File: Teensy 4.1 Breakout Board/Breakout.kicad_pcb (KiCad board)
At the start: 2 copper layers, 145 x 64.5 mm, 20 parts, among them J1 CAN1, J2 CAN2, J3 12V_IN, J4 APPS, J5 BRAKE_PRESSURE_IN, J6 BRAKE_LIGHT_OUT, J7 3.3V_OUT, J8 GND_COMMON, M3 MountingHole_3.2mm_M3_Pad, Q1 IRLZ44N, U1 Teensy4.1, U2 MCP2562-E-P, U3 LM2596S-5, U4 MCP2562-E-P

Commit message: breakout board v1 sizing
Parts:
- removed M3 (x4): MountingHole_3.2mm_M3_Pad, MountingHole:MountingHole_3.2mm_M3_Pad
- removed U4: MCP2562-E-P, Package_DIP:DIP-8_W7.62mm
- added C1: 0.1uF, FA14_Capacitor:FA18X7R1H104KNU00, F.Cu at (156.3, 88.0)
- added C15: 220uF, Capacitor_THT:CP_Radial_D6.3mm_P2.50mm, F.Cu at (151.3, 113.6)
- added C18: 680uF, footprints:CAPPRD500W60D1275H2700, F.Cu at (163.4, 123.8)
- added C2: 0.1uF, FA14_Capacitor:FA18X7R1H104KNU00, F.Cu at (192.1, 114.2)
- added C3: 0.1uF, FA14_Capacitor:FA18X7R1H104KNU00, F.Cu at (152.5, 89.9)
- added C5: 0.1uF, FA14_Capacitor:FA18X7R1H104KNU00, F.Cu at (182.0, 90.5)
- added C6: 0.1uF, FA14_Capacitor:FA18X7R1H104KNU00, F.Cu at (178.5, 90.5)
- added C7: 0.1uF, FA14_Capacitor:FA18X7R1H104KNU00, F.Cu at (175.0, 90.5)
- added C8: 0.1uF, FA14_Capacitor:FA18X7R1H104KNU00, F.Cu at (171.5, 90.5)
- added C9: 10uF, Capacitor_THT:CP_Radial_D5.0mm_P2.50mm, F.Cu at (152.6, 85.3)
- added D1: NUP3105L, Package_TO_SOT_SMD:SOT-23, F.Cu at (156.7, 84.6)
- added D3: 1N5821, Diode_THT:D_DO-201AD_P15.24mm_Horizontal, F.Cu at (176.8, 134.3)
- added J10: RTD_Speaker, Connector_JST:JST_XH_B2B-XH-A_1x02_P2.50mm_Vertical, F.Cu at (187.8, 118.9)
- added J9: Brake_Light, Connector_JST:JST_XH_B2B-XH-A_1x02_P2.50mm_Vertical, F.Cu at (187.8, 126.3)
- added JP1: SolderJumper_2_Open, Jumper:SolderJumper-2_P1.3mm_Open_Pad1.0x1.5mm, F.Cu at (167.8, 89.3)
- added L1: 33uH, Inductor_SMD:L_10.4x10.4_H4.8, F.Cu at (178.8, 123.7)
- added Q2: 2N7000, Package_TO_SOT_THT:TO-92_Inline, F.Cu at (187.7, 114.2)
- added R10: 20k, Resistor_THT:R_Axial_DIN0207_L6.3mm_D2.5mm_P10.16mm_Horizontal, F.Cu at (186.5, 82.5)
- added R11: 10k, Resistor_THT:R_Axial_DIN0207_L6.3mm_D2.5mm_P10.16mm_Horizontal, F.Cu at (209.7, 86.0)
- added R12: 20k, Resistor_THT:R_Axial_DIN0207_L6.3mm_D2.5mm_P10.16mm_Horizontal, F.Cu at (199.5, 89.5)
- added R13: 1k, Resistor_THT:R_Axial_DIN0207_L6.3mm_D2.5mm_P10.16mm_Horizontal, F.Cu at (183.7, 78.0)
- added R14: 1k, Resistor_THT:R_Axial_DIN0207_L6.3mm_D2.5mm_P10.16mm_Horizontal, F.Cu at (183.7, 81.5)
- added R15: 1k, Resistor_THT:R_Axial_DIN0207_L6.3mm_D2.5mm_P10.16mm_Horizontal, F.Cu at (183.7, 85.0)
- added R16: 1k, Resistor_THT:R_Axial_DIN0207_L6.3mm_D2.5mm_P10.16mm_Horizontal, F.Cu at (170.7, 80.1)
- added R4: 20k, Resistor_THT:R_Axial_DIN0207_L6.3mm_D2.5mm_P10.16mm_Horizontal, F.Cu at (199.4, 82.5)
- added R5: 100, Resistor_THT:R_Axial_DIN0207_L6.3mm_D2.5mm_P10.16mm_Horizontal, F.Cu at (155.0, 111.9)
- added R6: 100k, Resistor_THT:R_Axial_DIN0207_L6.3mm_D2.5mm_P10.16mm_Horizontal, F.Cu at (155.0, 115.4)
- added R7: 100, Resistor_THT:R_Axial_DIN0207_L6.3mm_D2.5mm_P10.16mm_Horizontal, F.Cu at (173.1, 112.3)
- added R8: 100k, Resistor_THT:R_Axial_DIN0207_L6.3mm_D2.5mm_P10.16mm_Horizontal, F.Cu at (173.1, 115.7)
- added R9: 10k, Resistor_THT:R_Axial_DIN0207_L6.3mm_D2.5mm_P10.16mm_Horizontal, F.Cu at (196.7, 79.0)
- added REF**: MountingHole_3.2mm_M3, MountingHole:MountingHole_3.2mm_M3, F.Cu at (143.4, 100.8)
- added REF**: MountingHole_3.2mm_M3, MountingHole:MountingHole_3.2mm_M3, F.Cu at (143.4, 79.3)
- added REF**: MountingHole_3.2mm_M3, MountingHole:MountingHole_3.2mm_M3, F.Cu at (214.8, 100.8)
- added REF**: MountingHole_3.2mm_M3, MountingHole:MountingHole_3.2mm_M3, F.Cu at (143.4, 133.6)
- added REF**: MountingHole_3.2mm_M3, MountingHole:MountingHole_3.2mm_M3, F.Cu at (214.8, 133.6)
- added REF**: MountingHole_2.7mm_M2.5, MountingHole:MountingHole_2.7mm_M2.5, F.Cu at (208.1, 113.0)
- added REF**: MountingHole_3.2mm_M3, MountingHole:MountingHole_3.2mm_M3, F.Cu at (214.8, 79.3)
- added REF**: MountingHole_2.7mm_M2.5, MountingHole:MountingHole_2.7mm_M2.5, F.Cu at (208.1, 129.0)
- added R_CAN_TERM1: 120, Resistor_THT:R_Axial_DIN0207_L6.3mm_D2.5mm_P10.16mm_Horizontal, F.Cu at (160.5, 83.7)
- added U26: LM2596SX-5.0/NOPB, Package_TO_SOT_SMD:TO-263-5_TabPin3, F.Cu at (153.1, 128.7)
- J1: value CAN1 -> CAN; footprint TerminalBlock_Phoenix:TerminalBlock_Phoenix_MKDS-1,5-2-5.08_1x02_P5.08mm_Horizontal -> Connector_JST:JST_XH_B3B-XH-A_1x03_P2.50mm_Vertical
- J2: value CAN2 -> 12V Power; footprint TerminalBlock_Phoenix:TerminalBlock_Phoenix_MKDS-1,5-2-5.08_1x02_P5.08mm_Horizontal -> Connector_JST:JST_XH_B2B-XH-A_1x02_P2.50mm_Vertical
- J3: value 12V_IN -> APPS1; footprint TerminalBlock_Phoenix:TerminalBlock_Phoenix_MKDS-1,5-2-5.08_1x02_P5.08mm_Horizontal -> Connector_JST:JST_XH_B3B-XH-A_1x03_P2.50mm_Vertical
- J4: value APPS -> APPS2; footprint TerminalBlock_Phoenix:TerminalBlock_Phoenix_MKDS-1,5-2-5.08_1x02_P5.08mm_Horizontal -> Connector_JST:JST_XH_B3B-XH-A_1x03_P2.50mm_Vertical
- J5: value BRAKE_PRESSURE_IN -> Brake_Pressure_Front; footprint TerminalBlock_Phoenix:TerminalBlock_Phoenix_MKDS-1,5-2-5.08_1x02_P5.08mm_Horizontal -> Connector_JST:JST_XH_B3B-XH-A_1x03_P2.50mm_Vertical
- J6: value BRAKE_LIGHT_OUT -> Brake_Pressure_Rear; footprint TerminalBlock_Phoenix:TerminalBlock_Phoenix_MKDS-1,5-2-5.08_1x02_P5.08mm_Horizontal -> Connector_JST:JST_XH_B3B-XH-A_1x03_P2.50mm_Vertical
- J7: value 3.3V_OUT -> Nextion; footprint TerminalBlock_Phoenix:TerminalBlock_Phoenix_MKDS-1,5-4-5.08_1x04_P5.08mm_Horizontal -> Connector_JST:JST_XH_B4B-XH-A_1x04_P2.50mm_Vertical
- J8: value GND_COMMON -> ESP32; footprint TerminalBlock_Phoenix:TerminalBlock_Phoenix_MKDS-1,5-4-5.08_1x04_P5.08mm_Horizontal -> Connector_JST:JST_XH_B4B-XH-A_1x04_P2.50mm_Vertical
- Q1: value IRLZ44N -> 2N7000; footprint Package_TO_SOT_THT:TO-220-3_Vertical -> Package_TO_SOT_THT:TO-92_Inline
- R1: value 120 -> 10k; footprint Resistor_SMD:R_0603_1608Metric -> Resistor_THT:R_Axial_DIN0207_L6.3mm_D2.5mm_P10.16mm_Horizontal
- R2: value 120 -> 20k; footprint Resistor_SMD:R_0603_1608Metric -> Resistor_THT:R_Axial_DIN0207_L6.3mm_D2.5mm_P10.16mm_Horizontal
- R3: value 10K -> 10k; footprint Resistor_SMD:R_0603_1608Metric -> Resistor_THT:R_Axial_DIN0207_L6.3mm_D2.5mm_P10.16mm_Horizontal
- U1: value Teensy4.1 -> SN65HVD230; footprint teensy:Teensy41 -> Package_SO:SOIC-8_3.9x4.9mm_P1.27mm
- U2: value MCP2562-E-P -> module_mpu6050; footprint Package_DIP:DIP-8_W7.62mm -> usini_sensors:module_mpu6050
- U3: value LM2596S-5 -> Teensy4.1; footprint Package_TO_SOT_SMD:TO-263-5_TabPin3 -> teensy.pretty-master:Teensy41
- moved J3 188.6 mm to (214.5, 125.2), turned to 90 degrees
- moved R2 148.6 mm to (186.5, 89.5)
- moved R1 143.1 mm to (196.7, 86.0), turned to 180 degrees
- moved U2 141.7 mm to (195.4, 130.0), turned to 0 degrees
- moved U3 128.8 mm to (179.3, 100.8), turned to 0 degrees
- moved J6 121.9 mm to (214.7, 91.9), turned to 90 degrees
- moved J4 119.6 mm to (214.5, 113.7), turned to 90 degrees
- moved J2 109.6 mm to (143.3, 123.0), turned to -90 degrees
- moved J1 106.7 mm to (155.6, 79.1), turned to 180 degrees
- moved J8 95.9 mm to (183.0, 133.9), turned to 0 degrees
- moved U1 60.3 mm to (162.3, 88.4), turned to 0 degrees
- moved R3 58.9 mm to (209.5, 79.0), turned to 180 degrees
- moved J5 39.0 mm to (144.2, 86.8), turned to -90 degrees
- moved Q1 37.5 mm to (169.5, 114.9), turned to 90 degrees
- moved J7 8.22 mm to (143.3, 108.9), turned to -90 degrees
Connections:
- J1 pad 1: Net-(J1-Pin_1) -> CAN_GND
- J1 pad 2: Net-(J1-Pin_2) -> CANL
- J2 pad 1: Net-(J2-Pin_1) -> 12V
- J2 pad 2: Net-(J2-Pin_2) -> CAN_GND
- J3 pad 1: Net-(J3-Pin_1) -> 5V
- J3 pad 2: /BRAKE_LIGHT_12V -> APPS1
- J4 pad 1: /APPS1 -> 5V
- J4 pad 2: /APPS2 -> APPS2
- J5 pad 1: /FRONT_BRAKE_PRESSURE -> 5V
- J5 pad 2: /REAR_BRAKE_PRESSURE -> Brake_Front
- J6 pad 1: Net-(J6-Pin_1) -> 5V
- J6 pad 2: /BRAKE_LIGHT_12V -> Brake_Rear
- J7 pad 1: /3.3V -> 5V
- J7 pad 2: /3.3V -> Nextion_TX
- J7 pad 3: /3.3V -> Nextion_RX
- J7 pad 4: /3.3V -> CAN_GND
- J8 pad 1: /GND -> 5V
- J8 pad 2: /GND -> ESP32_TX
- J8 pad 3: /GND -> ESP32_RX
- J8 pad 4: /GND -> CAN_GND
- Q1 pad 1: /BRAKE_LIGHT_CONTROL -> CAN_GND
- Q1 pad 2: Net-(J6-Pin_1) -> Net-(Q1-G)
- Q1 pad 3: /GND -> Net-(J9-Pin_2)
- R1 pad 1: Net-(J1-Pin_1) -> APPS1
- R1 pad 2: Net-(J1-Pin_2) -> Net-(R1-Pad2)
- R2 pad 1: Net-(J2-Pin_1) -> Net-(R1-Pad2)
- R2 pad 2: Net-(J2-Pin_2) -> CAN_GND
- R3 pad 1: /GND -> APPS2
- R3 pad 2: /BRAKE_LIGHT_CONTROL -> Net-(R14-Pad2)
- U1 pad 1: /GND -> CAN1_TX
- U1 pad 2: /CAN2_RX -> CAN_GND
- U1 pad 3: /CAN2_TX -> 3.3V
- U1 pad 4: /BRAKE_LIGHT_CONTROL -> CAN1_RX
- U1 pad 6: unconnected-(U1-4_BCLK2-Pad6) -> CANL
- U1 pad 7: unconnected-(U1-5_IN2-Pad7) -> CANH
- U1 pad 8: unconnected-(U1-6_OUT1D-Pad8) -> CAN_GND
- U2 pad 1: /CAN1_TX -> 3.3V
- U2 pad 2: /GND -> CAN_GND
- U2 pad 3: /5V -> MPU_SCL
- U2 pad 4: /CAN1_RX -> MPU_SDA
- U2 pad 5: /3.3V -> unconnected-(U2-XDA-Pad5)
- U2 pad 6: Net-(J1-Pin_2) -> unconnected-(U2-XCL-Pad6)
- U2 pad 7: Net-(J1-Pin_1) -> unconnected-(U2-ADD-Pad7)
- U2 pad 8: /GND -> unconnected-(U2-INT-Pad8)
- U3 pad 1: /BRAKE_LIGHT_12V -> unconnected-(U3-GND-Pad1)
- U3 pad 2: /5V -> Nextion_TX
- U3 pad 3: Net-(J3-Pin_1) -> Nextion_RX
- U3 pad 5: Net-(J3-Pin_1) -> unconnected-(U3-3_LRCLK2-Pad5)
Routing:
- net /5V: track 273.5 -> 0.00 mm
- net /GND: track 165.2 -> 0.00 mm
- net /CAN1_RX: track 149.8 -> 0.00 mm
- net /3.3V: track 132.8 -> 0.00 mm
- net /CAN2_RX: track 127.3 -> 0.00 mm
- net /CAN2_TX: track 110.3 -> 0.00 mm
- net Net-(J6-Pin_1): track 64.9 -> 0.00 mm
- net /BRAKE_LIGHT_12V: track 63.4 -> 0.00 mm
- net /CAN1_TX: track 62.3 -> 0.00 mm
- net /BRAKE_LIGHT_CONTROL: track 45.7 -> 0.00 mm
- net Net-(J3-Pin_1): track 27.1 -> 0.00 mm
- net Net-(J2-Pin_2): track 25.1 -> 0.00 mm
- net Net-(J2-Pin_1): track 21.3 -> 0.00 mm
- net /APPS1: track 17.9 -> 0.00 mm
- net /REAR_BRAKE_PRESSURE: track 17.2 -> 0.00 mm
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- added copper zone on F.Cu, net CAN_GND
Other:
- board size 145 x 64.5 mm -> 81.4 x 64.3 mm
- board text removed: "UCDFS TEENSY 4.1 BREAKOUT BOARD"

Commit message: breakout complete
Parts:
- moved R5 10.2 mm to (165.2, 111.9), turned to 180 degrees
- moved Q1 2.71 mm to (168.9, 112.3), turned to -90 degrees
- moved C9 2.71 mm to (149.9, 85.4), turned to 0 degrees
- moved Q2 2.50 mm to (187.3, 111.7), turned to -90 degrees
- moved C15 2.48 mm to (148.8, 113.6), turned to 0 degrees
- moved C5 0.22 mm to (182.2, 90.4)
- moved C6 0.22 mm to (178.7, 90.4)
- moved C7 0.22 mm to (175.2, 90.4)
- moved C8 0.22 mm to (171.7, 90.4)
- moved R6 0.10 mm to (155.0, 115.3)
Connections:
- J1 pad 2: CANL -> CANH
- J1 pad 3: CANH -> CANL
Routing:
- net 5V: track 0.00 -> 170.7 mm
- net Brake_Front: track 0.00 -> 60.9 mm
- net 3.3V: track 0.00 -> 60.5 mm
- net 12V: track 0.00 -> 57.6 mm
- net APPS1: track 0.00 -> 48.3 mm
- net Net-(R11-Pad2): track 0.00 -> 48.0 mm
- net MPU_SDA: track 0.00 -> 45.8 mm
- net MPU_SCL: track 0.00 -> 43.8 mm
- net Net-(D3-K): track 0.00 -> 38.1 mm
- net APPS2: track 0.00 -> 34.3 mm
- net ESP32_TX: track 0.00 -> 32.3 mm
- net ESP32_RX: track 0.00 -> 31.7 mm
- net Net-(R14-Pad2): track 0.00 -> 30.9 mm
- net Net-(J9-Pin_2): track 0.00 -> 26.6 mm
- net CANL: track 0.00 -> 22.9 mm
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
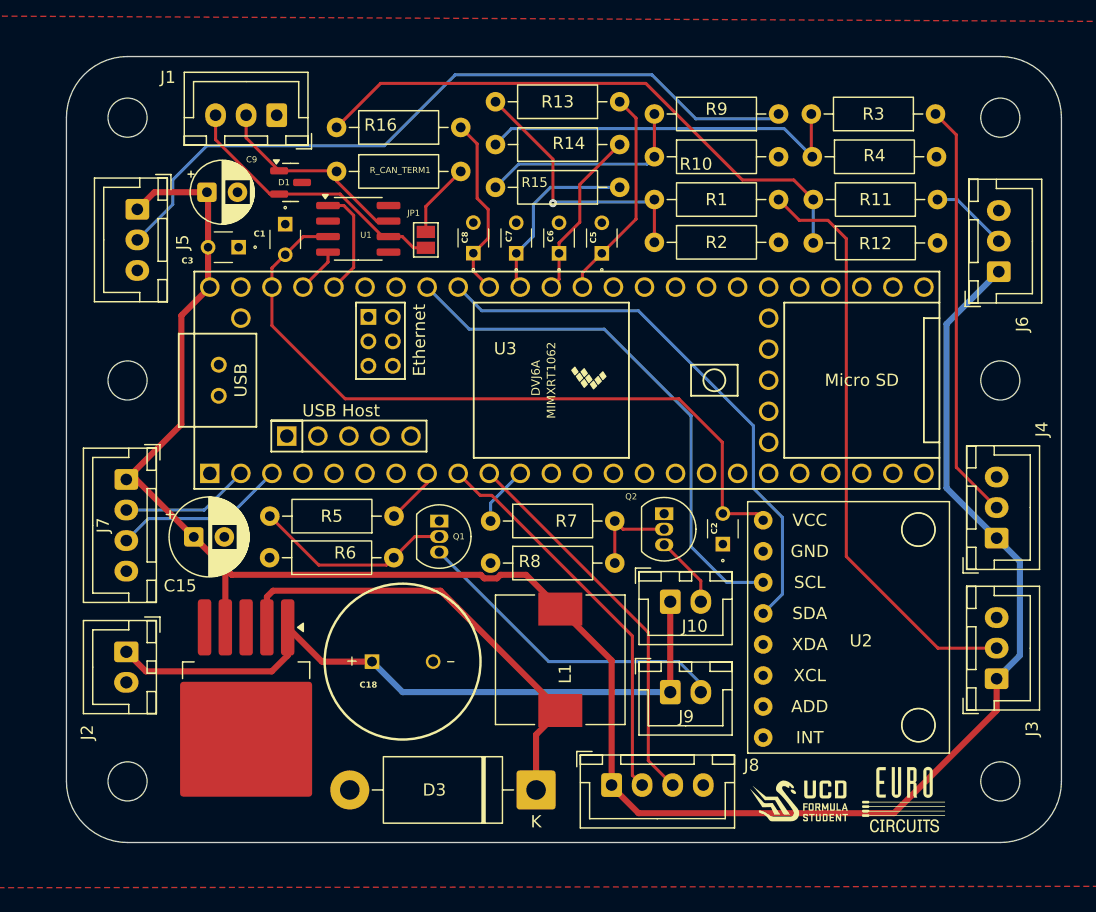
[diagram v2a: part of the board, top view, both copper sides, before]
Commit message: breakout updated and ENNOID BMS added
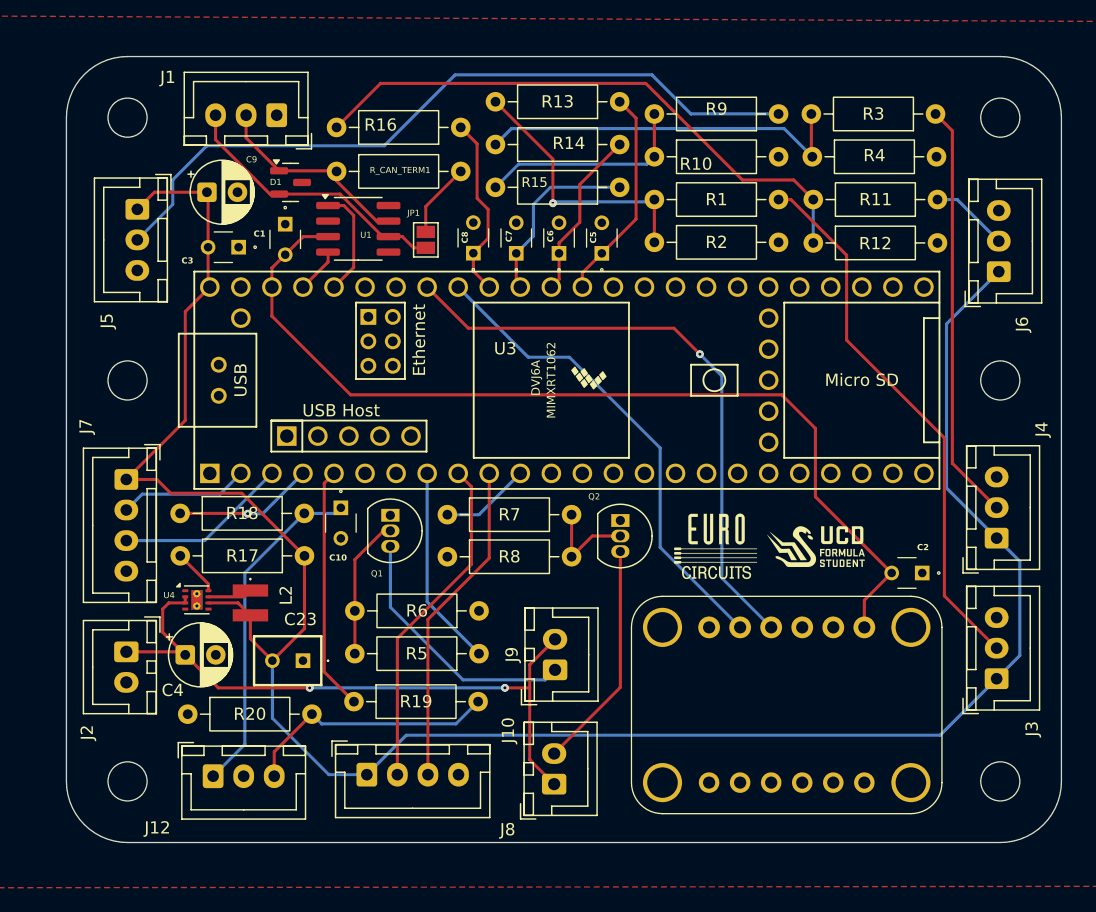
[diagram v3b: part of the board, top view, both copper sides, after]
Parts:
- removed C15: 220uF, Capacitor_THT:CP_Radial_D6.3mm_P2.50mm
- removed C18: 680uF, footprints:CAPPRD500W60D1275H2700
- removed D3: 1N5821, Diode_THT:D_DO-201AD_P15.24mm_Horizontal
- removed L1: 33uH, Inductor_SMD:L_10.4x10.4_H4.8
- removed the REF** at (208.1, 113.0)
- removed the REF** at (208.1, 129.0)
- removed U2: module_mpu6050, usini_sensors:module_mpu6050
- removed U26: LM2596SX-5.0/NOPB, Package_TO_SOT_SMD:TO-263-5_TabPin3
- added C10: 0.1uF, FA14_Capacitor:FA18X7R1H104KNU00, F.Cu at (160.8, 111.2)
- added C23: 22uF, RDEC71E:RDEC71E226K3P1H03B, F.Cu at (157.8, 123.7)
- added C4: 10uF, Capacitor_THT:CP_Radial_D5.0mm_P2.50mm, F.Cu at (148.1, 123.2)
- added J12: RTD_button, Connector_JST:JST_XH_B3B-XH-A_1x03_P2.50mm_Vertical, F.Cu at (150.4, 133.2)
- added L2: 2.2uH, XFL3012222:XFL3012222MEC, F.Cu at (153.4, 119.0)
- added R17: 100k, Resistor_THT:R_Axial_DIN0207_L6.3mm_D2.5mm_P10.16mm_Horizontal, F.Cu at (157.9, 115.2)
- added R18: 220, Resistor_THT:R_Axial_DIN0207_L6.3mm_D2.5mm_P10.16mm_Horizontal, F.Cu at (147.7, 111.7)
- added R19: 100, Resistor_THT:R_Axial_DIN0207_L6.3mm_D2.5mm_P10.16mm_Horizontal, F.Cu at (161.9, 127.1)
- added R20: 100k, Resistor_THT:R_Axial_DIN0207_L6.3mm_D2.5mm_P10.16mm_Horizontal, F.Cu at (148.3, 128.1)
- added U4: TPS62163DSG, Package_SON:WSON-8-1EP_2x2mm_P0.5mm_EP0.9x1.6mm_ThermalVias, F.Cu at (149.1, 118.8)
- added U5: MPU6050, adafruit:MPU6050, F.Cu at (200.7, 129.6)
- moved J8 20.0 mm to (163.0, 133.1)
- moved J10 17.7 mm to (178.3, 133.8), turned to 90 degrees
- moved R6 17.7 mm to (172.2, 119.7), turned to 180 degrees
- moved C2 16.5 mm to (208.4, 116.5), turned to 180 degrees
- moved R5 13.2 mm to (172.2, 123.2)
- moved J9 9.60 mm to (178.4, 124.5), turned to 90 degrees
- moved Q1 4.03 mm to (164.9, 111.8)
- moved Q2 3.63 mm to (183.7, 112.3)
- moved R7 3.57 mm to (169.6, 111.8)
- moved R8 3.57 mm to (169.6, 115.2)
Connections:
- J9 pad 1: 12V -> Net-(J9-Pin_1)
- J9 pad 2: Net-(J9-Pin_2) -> 12V
- Q1 pad 3: Net-(J9-Pin_2) -> Net-(J9-Pin_1)
- U3 pad 4: unconnected-(U3-2_OUT2-Pad4) -> RTD_button
- U3 pad 5: unconnected-(U3-3_LRCLK2-Pad5) -> Precharge_EN
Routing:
- net Net-(D3-K): track 38.1 -> 0.00 mm
- net Net-(J12-Pin_1): track 0.00 -> 27.8 mm
- net Net-(J9-Pin_2): track 26.6 -> 0.00 mm
- net Net-(J9-Pin_1): track 0.00 -> 21.3 mm
- net Net-(J12-Pin_3): track 0.00 -> 21.0 mm
- net Precharge_EN: track 0.00 -> 20.0 mm
- net 3.3V: track 60.5 -> 77.6 mm
- net Net-(J10-Pin_2): track 5.93 -> 18.8 mm
- net Brake_Light_EN: track 4.62 -> 16.5 mm
- net RTD_button: track 0.00 -> 11.4 mm, vias 0 -> 1
- net MPU_SDA: track 45.8 -> 39.4 mm
- net MPU_SCL: track 43.8 -> 49.4 mm, vias 0 -> 1
- net ESP32_RX: track 31.7 -> 26.7 mm
- net Net-(Q1-G): track 16.5 -> 11.6 mm
- net ESP32_TX: track 32.3 -> 27.6 mm
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
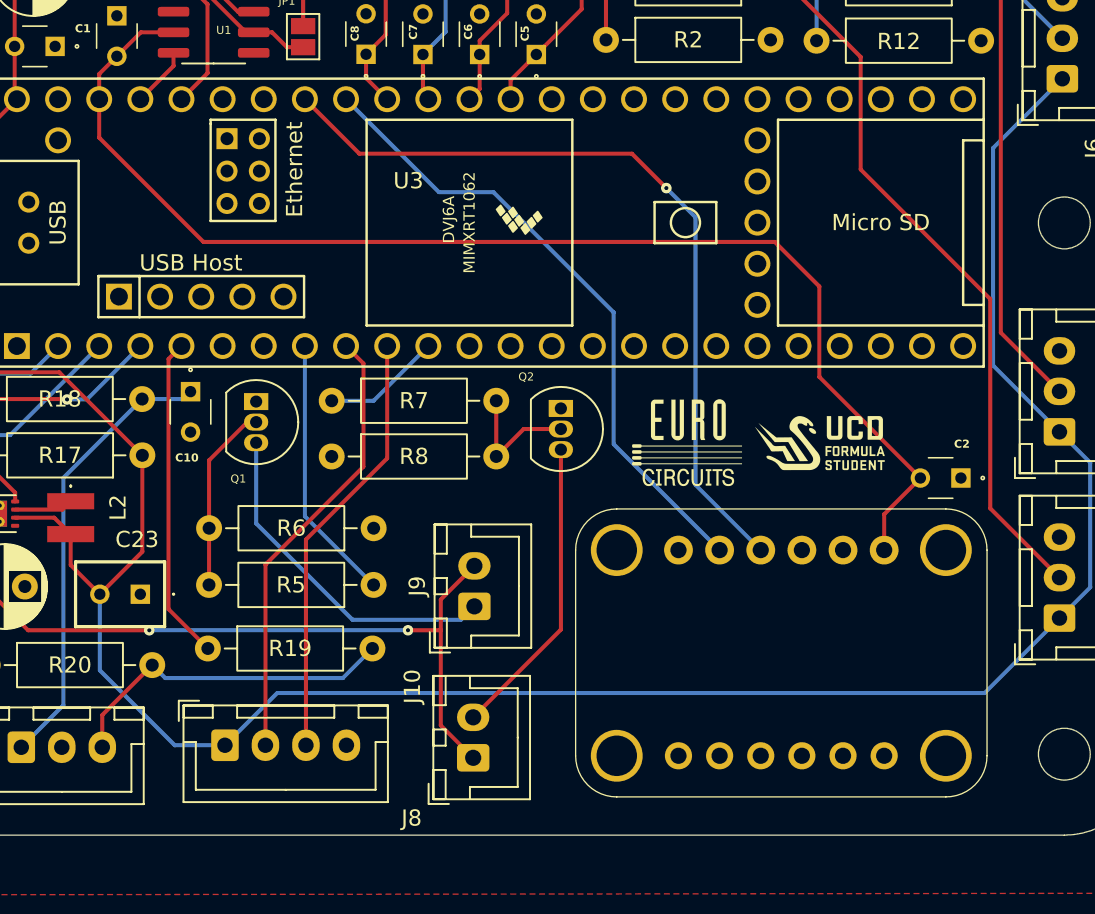
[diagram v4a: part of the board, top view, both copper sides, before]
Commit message: updated breakout
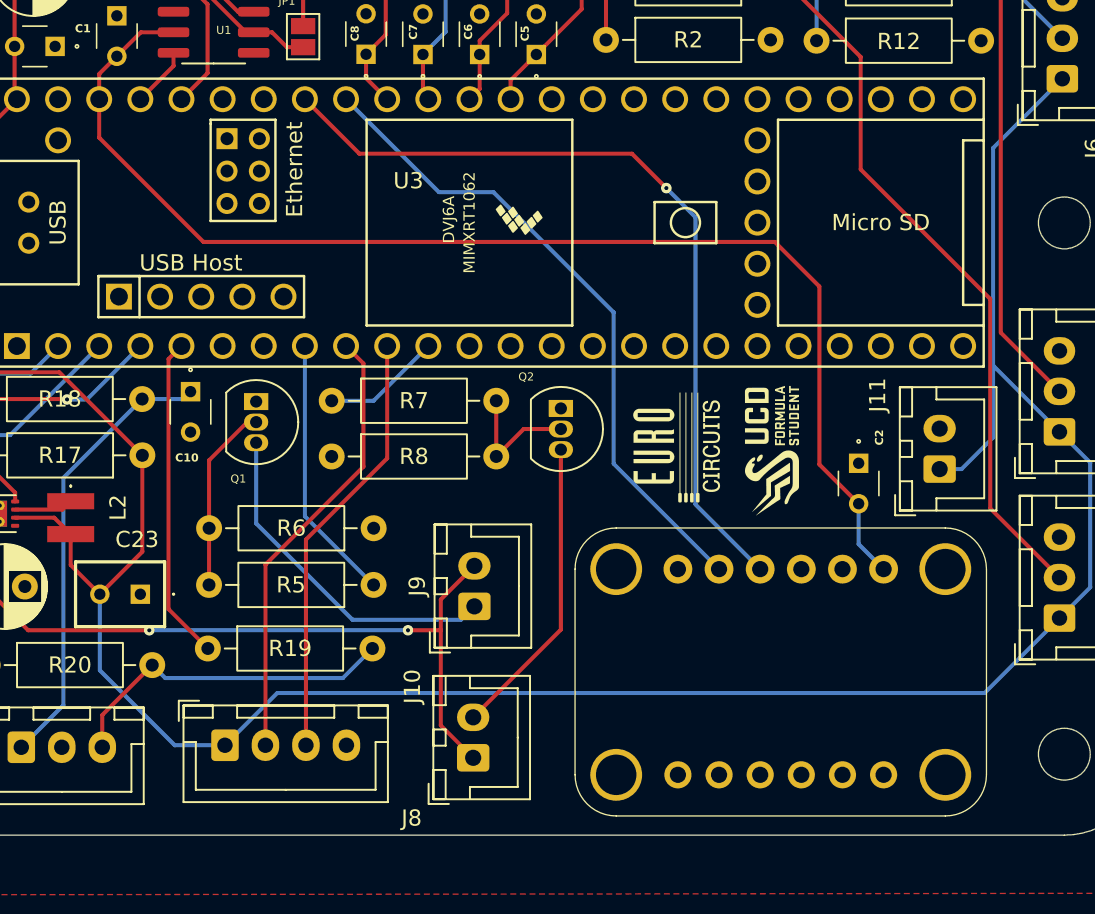
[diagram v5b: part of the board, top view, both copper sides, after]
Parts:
- added J11: Current Sensor Power source, Connector_JST:JST_XH_B2B-XH-A_1x02_P2.50mm_Vertical, F.Cu at (207.1, 116.0)
- moved C2 6.38 mm to (202.1, 115.6), turned to -90 degrees
- moved U5 1.18 mm to (200.6, 130.7)
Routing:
- net 5V: track 175.3 -> 183.9 mm
- net MPU_SDA: track 39.4 -> 40.5 mm
- net MPU_SCL: track 49.4 -> 50.5 mm
- net 3.3V: track 77.6 -> 77.0 mm
